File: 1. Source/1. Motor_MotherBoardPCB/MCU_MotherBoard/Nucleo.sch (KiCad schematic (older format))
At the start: 1 part

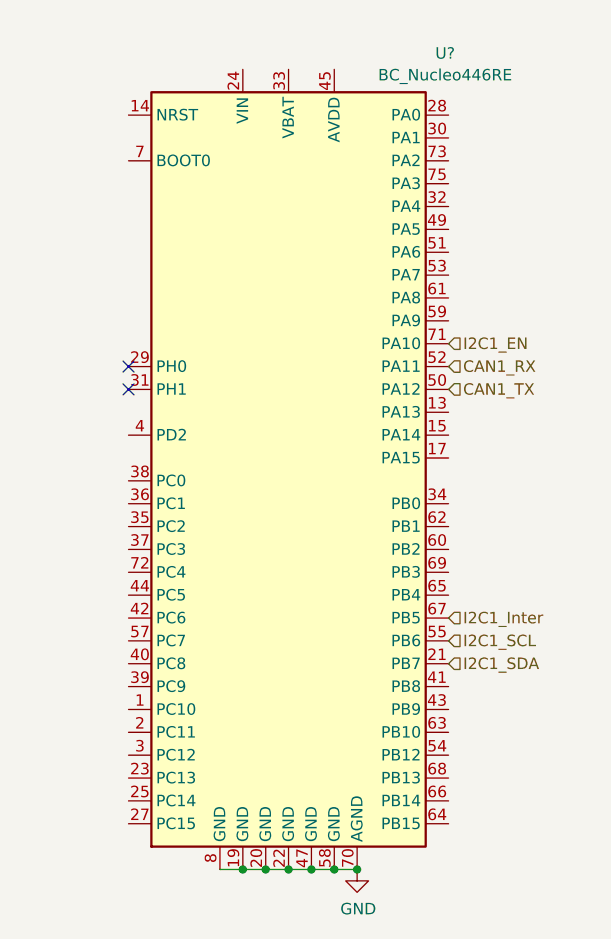
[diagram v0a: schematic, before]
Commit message: Add LoadCell_Click4 and SDCARD libraries
Add LoadCell_Click4 and SDCARD libraries
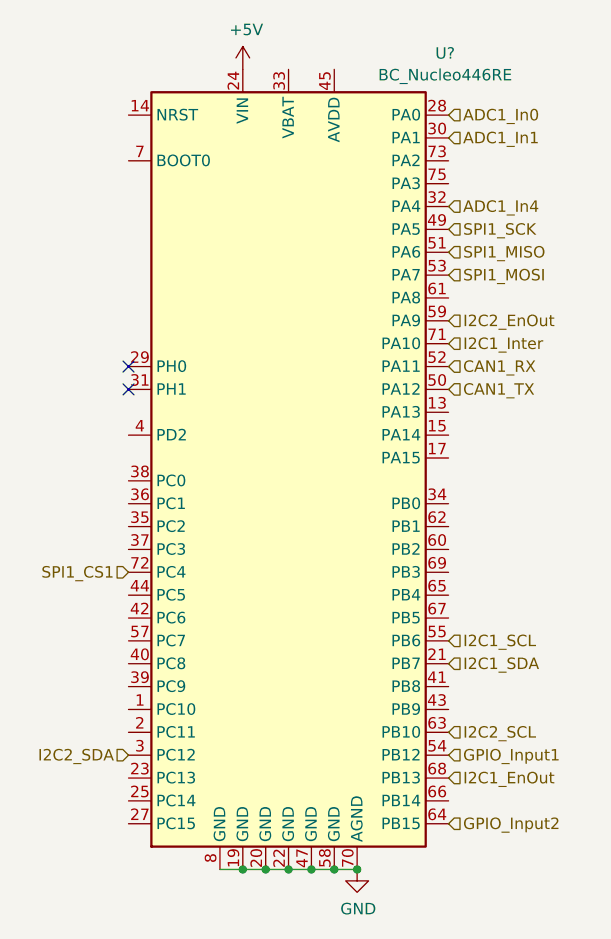
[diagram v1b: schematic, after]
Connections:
- net I2C1_EN is gone; now on net I2C1_Inter: U?.71 (PA10)
- net I2C1_Inter: no longer U?.67 (PB5)
- net +5V: now reaches U?.24 (VIN)
- net ADC1_In0: now reaches U?.28 (PA0)
- net I2C2_SDA: now reaches U?.3 (PC12)
- net ADC1_In1: now reaches U?.30 (PA1)
- net ADC1_In4: now reaches U?.32 (PA4)
- net SPI1_SCK: now reaches U?.49 (PA5)
- net SPI1_MISO: now reaches U?.51 (PA6)
- net SPI1_MOSI: now reaches U?.53 (PA7)
- net GPIO_Input1: now reaches U?.54 (PB12)
- net I2C2_EnOut: now reaches U?.59 (PA9)
- net I2C2_SCL: now reaches U?.63 (PB10)
- net GPIO_Input2: now reaches U?.64 (PB15)
- net I2C1_EnOut: now reaches U?.68 (PB13)
- net SPI1_CS1: now reaches U?.72 (PC4)
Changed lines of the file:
@@
 Text HLabel 5105 3660 2    50   Input ~ 0
 CAN1_TX
+Text HLabel 5105 5360 2    50   Input ~ 0
+I2C1_EnOut
 Text HLabel 5105 3460 2    50   Input ~ 0
-I2C1_EN
-Text HLabel 5105 4660 2    50   Input ~ 0
 I2C1_Inter
 Wire Wire Line
@@
 $EndComp
 Connection ~ 4705 5760
+$Comp
+L power:+5V #PWR?
+U 1 1 6385A94B
+P 4205 2260
+F 0 "#PWR?" H 4205 2110 50  0001 C CNN
+F 1 "+5V" H 4220 2433 50  0000 C CNN
+F 2 "" H 4205 2260 50  0001 C CNN
+F 3 "" H 4205 2260 50  0001 C CNN
+	1    4205 2260
+	1    0    0    -1
+$EndComp
+Text HLabel 5105 3360 2    50   Input ~ 0
+I2C2_EnOut
+Text HLabel 5105 5160 2    50   Input ~ 0
+I2C2_SCL
+Text HLabel 3705 5260 0    50   Input ~ 0
+I2C2_SDA
+Text HLabel 5105 2960 2    50   Input ~ 0
+SPI1_SCK
+Text HLabel 5105 3060 2    50   Input ~ 0
+SPI1_MISO
+Text HLabel 5105 3160 2    50   Input ~ 0
+SPI1_MOSI
+Text HLabel 3705 4460 0    50   Input ~ 0
+SPI1_CS1
+Text HLabel 5105 5260 2    50   Input ~ 0
+GPIO_Input1
+Text HLabel 5105 5560 2    50   Input ~ 0
+GPIO_Input2
+Text HLabel 5105 2460 2    50   Input ~ 0
+ADC1_In0
+Text HLabel 5105 2860 2    50   Input ~ 0
+ADC1_In4
+Text HLabel 5105 2560 2    50   Input ~ 0
+ADC1_In1
 $EndSCHEMATC
